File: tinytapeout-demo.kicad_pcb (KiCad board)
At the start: 4 copper layers, 99.5 x 78 mm, 319 parts, among them J1 Conn_01x06, J10 Conn_01x02, J11 Conn_01x06, J12 613012243121, J13 613012243121, J14 613012243121, J16 2x20_P2.54mm_Pinheader, J17 Conn_01x03, J18 2x20_P2.54mm_Pinheader, J19 Conn_01x02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

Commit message: v2.0.1
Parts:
- C16, C21: footprint Capacitor_SMD:C_0603_1608Metric -> Capacitor_SMD:C_0805_2012Metric
- R30: value 10k -> 5.1k
- moved C16 5.12 mm to (147.9, 71.2), turned to 90 degrees
- moved PSYLOGO1 1.08 mm to (87.8, 78.0)
- moved STITCHB1 0.60 mm to (84.1, 60.6)
- moved C21 0.52 mm to (90.3, 68.0)
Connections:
- R30 pad 2: GND -> +3V3
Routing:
- net +3V3: track 656.1 -> 661.0 mm, vias 62 -> 64
- net GND: track 171.2 -> 169.9 mm, vias 89 -> 88
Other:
- board text added: "v2.0.1"
- board text removed: "PWR"
- board text removed: "v2.0.0"

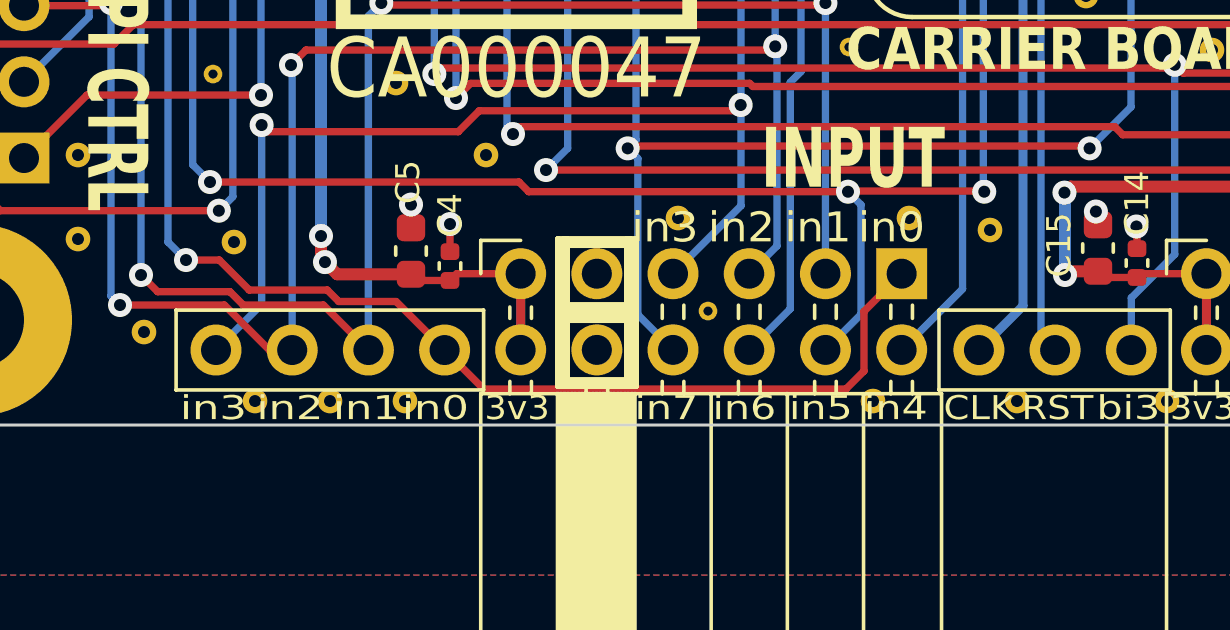
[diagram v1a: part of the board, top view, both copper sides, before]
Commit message: the great net rename
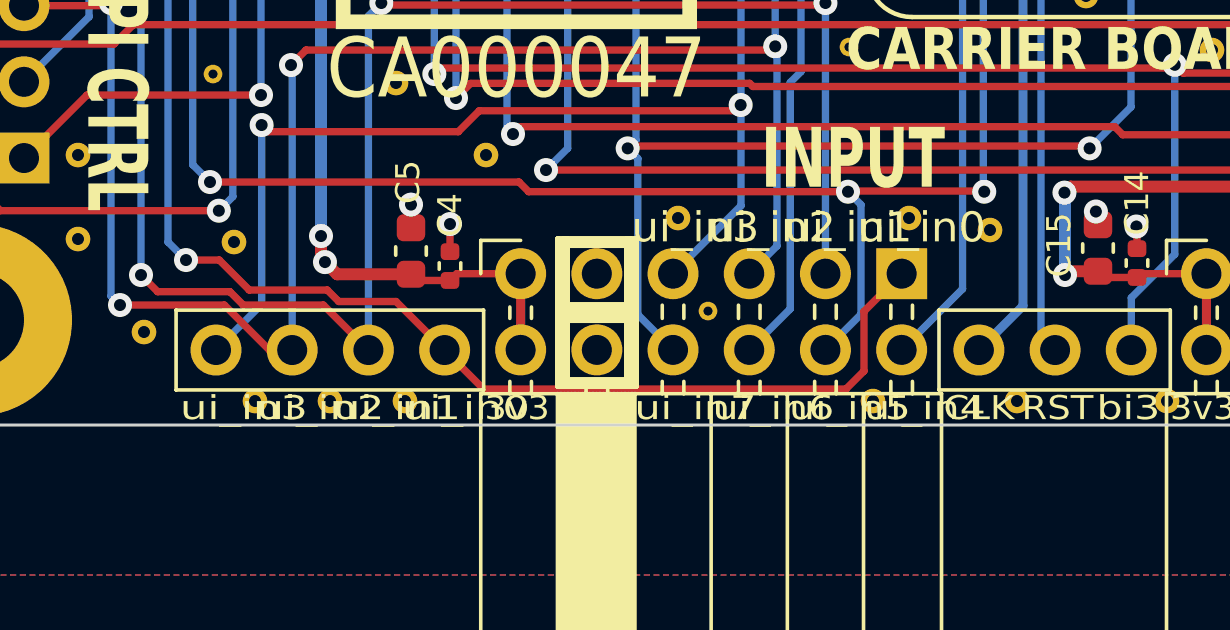
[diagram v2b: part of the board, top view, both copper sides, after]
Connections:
- net in0 renamed ui_in0
- net in1 renamed ui_in1
- net in2 renamed ui_in2
- net in3 renamed ui_in3
- net in4 renamed ui_in4
- net in5 renamed ui_in5
- net in6 renamed ui_in6
- net in7 renamed ui_in7
- net out0 renamed uo_out0
- net out1 renamed uo_out1
- net out2 renamed uo_out2
- net out3 renamed uo_out3
- net out4 renamed uo_out4
- net out5 renamed uo_out5
- net out6 renamed uo_out6
- net out7 renamed uo_out7
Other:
- board text added: "ui_in0"
- board text added: "ui_in1"
- board text added: "ui_in2"
- board text added: "ui_in3"
- board text added: "ui_in4"
- board text added: "ui_in5"
- board text added: "ui_in6"
- board text added: "ui_in7"
- board text removed: "in0"
- board text removed: "in1"
- board text removed: "in2"
- board text removed: "in3"
- board text removed: "in4"
- board text removed: "in5"
- board text removed: "in6"
- board text removed: "in7"

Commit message: the great relabelling
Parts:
- R42, R43, R44, R45, R46, R47, R48, R51, R52, R53, R54, R55: value 10k -> 1M
- moved TTLOGO2 1.79 mm to (147.6, 76.0)
- moved Z2ALOGO2 1.79 mm to (127.5, 75.9)
- moved OSHWLOGO2 1.00 mm to (87.5, 67.5)
- moved PSYLOGO1 1.00 mm to (87.8, 77.0)
- moved PSYLOGO2 0.73 mm to (147.0, 122.8)
- moved C25 0.40 mm to (88.1, 68.5)
- moved C21 0.30 mm to (90.0, 68.0)
- moved C11 0.10 mm to (114.7, 61.5)
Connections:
- J16 pad 1: unconnected-(J16-Pad1) -> GND
- J18 pad 1: unconnected-(J18-Pad1) -> uo_out6
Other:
- board text added: "RP2040 upgrades: * Hold BOOT button * Connect to USB * Release BOOT Should see an RPI-RP2 drive. Copy UF2 file over, that's it."
- board text added: "i0"
- board text added: "i1"
- board text added: "i2"
- board text added: "i3"
- board text added: "i4"
- board text added: "i5"
- board text added: "i6"
- board text added: "i7"
- board text added: "io0"
- board text added: "io1"
- board text added: "io2"
- board text added: "io3"
- board text added: "io4"
- board text added: "io5"
- board text added: "io6"
- board text added: "io7"
- board text added: "o0"
- board text added: "o1"
- board text added: "o2"
- board text added: "o3"
- board text added: "o4"
- board text added: "o5"
- board text added: "o6"
- board text added: "o7"
- board text added: "ui_in"
- board text added: "uio"
- board text added: "uo_out"
- board text added: "v2.1.0"
- board text removed: "RP2040 upgrades: * Hold BOOT button * Connect to USB * Release BOOT Should see an RPI-RP2 drive. Copy UF2 file over, done."
- board text removed: "bi0"
- board text removed: "bi1"
- board text removed: "bi2"
- board text removed: "bi3"
- board text removed: "bi4"
- board text removed: "bi5"
- board text removed: "bi6"
- board text removed: "bi7"
- board text removed: "ot0"
- board text removed: "ot1"
- board text removed: "ot2"
- board text removed: "ot3"
- board text removed: "ot4"
- board text removed: "ot5"
- board text removed: "ot6"
- board text removed: "ot7"
- board text removed: "ui_in0"
- board text removed: "ui_in1"
- board text removed: "ui_in2"
- board text removed: "ui_in3"
- board text removed: "ui_in4"
- board text removed: "ui_in5"
- board text removed: "ui_in6"
- board text removed: "ui_in7"
- board text removed: "v2.0.1"
